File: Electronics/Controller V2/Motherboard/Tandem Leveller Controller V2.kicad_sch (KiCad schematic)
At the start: 6 parts, among them J8 776180-1, J9 776279-1

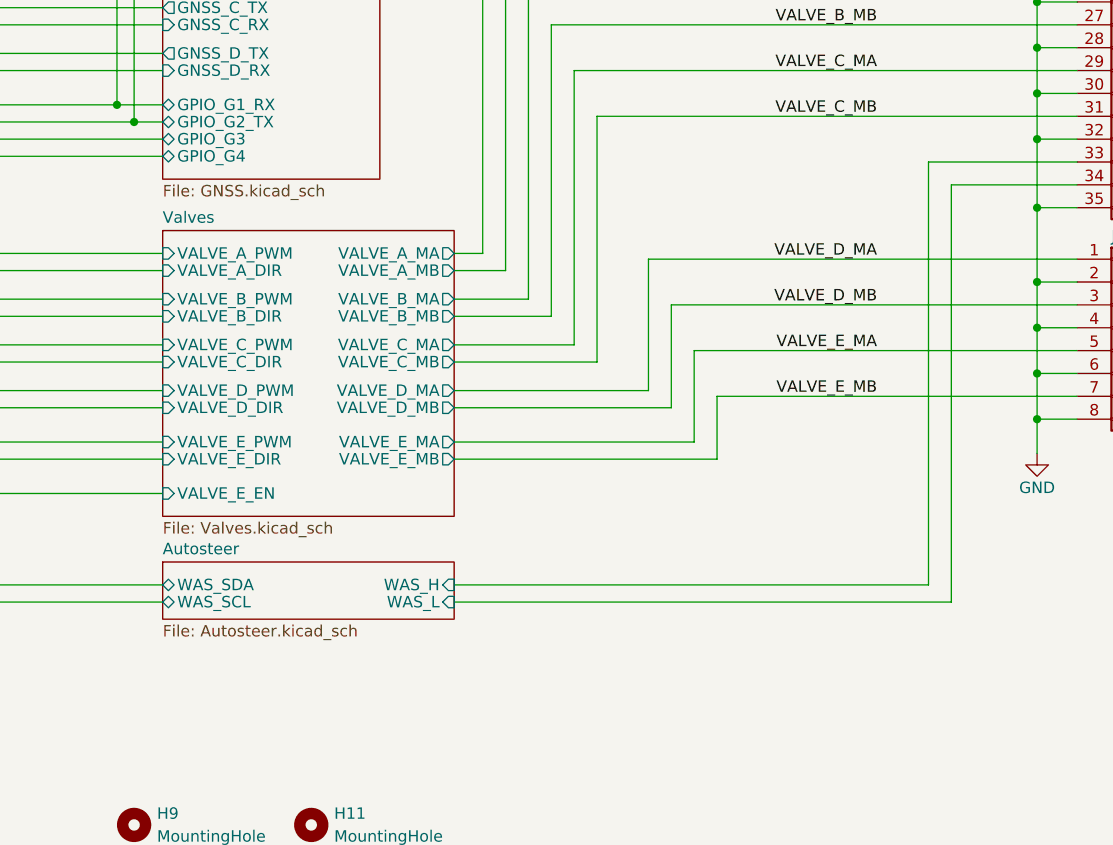
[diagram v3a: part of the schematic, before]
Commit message: Added current sensing for valve E.
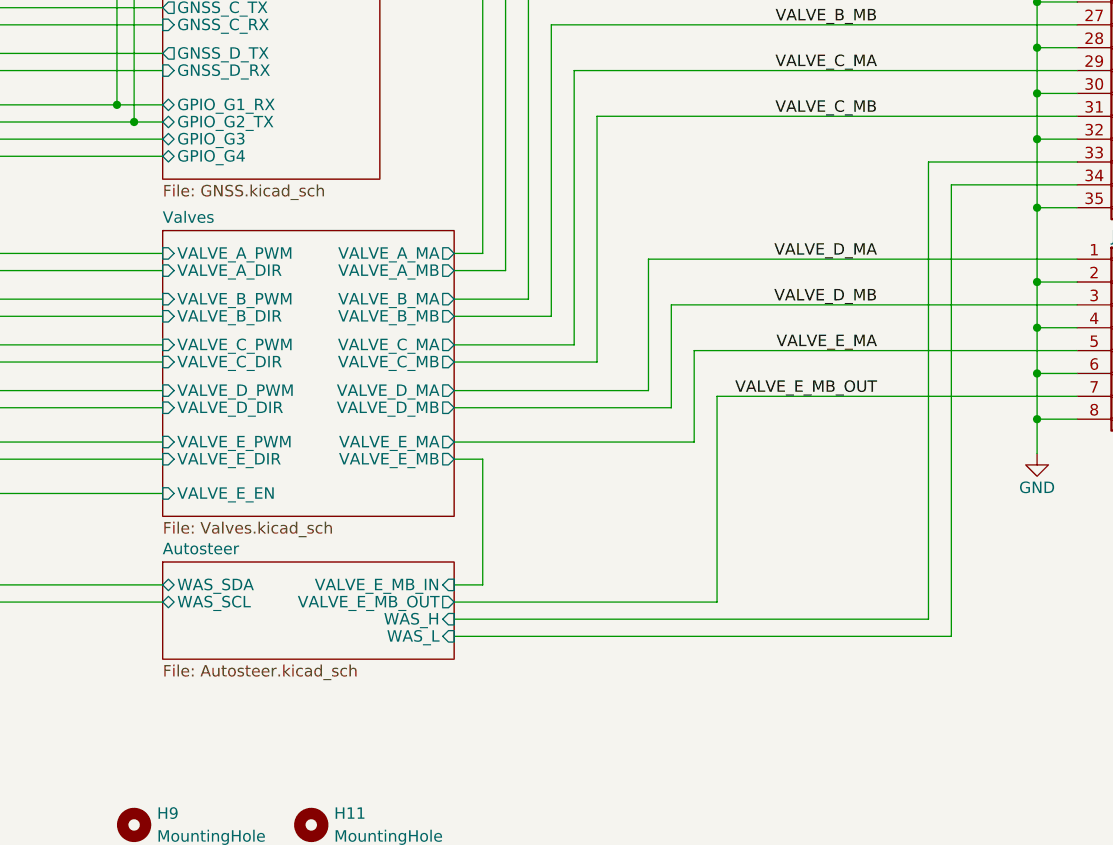
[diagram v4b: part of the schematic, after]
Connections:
- net VALVE_E_MB renamed VALVE_E_MB_OUT
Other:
- sheet Autosteer ports: added VALVE_E_MB_IN, VALVE_E_MB_OUT; removed none
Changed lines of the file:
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@@
     (stroke (width 0) (type default))
   )
-  (wire (pts (xy 222.885 114.3) (xy 222.885 160.655))
+  (wire (pts (xy 222.885 114.3) (xy 222.885 164.465))
     (stroke (width 0) (type default))
   )
@@
     (stroke (width 0) (type default))
   )
+  (wire (pts (xy 167.64 160.655) (xy 196.85 160.655))
+    (stroke (width 0) (type default))
+  )
   (wire (pts (xy 232.41 43.18) (xy 236.855 43.18))
     (stroke (width 0) (type default))
   )
-  (wire (pts (xy 222.885 160.655) (xy 167.64 160.655))
+  (wire (pts (xy 222.885 164.465) (xy 167.64 164.465))
     (stroke (width 0) (type default))
   )
@@
     (stroke (width 0) (type default))
   )
+  (wire (pts (xy 170.815 158.75) (xy 167.64 158.75))
+    (stroke (width 0) (type default))
+  )
   (wire (pts (xy 160.02 38.1) (xy 222.885 38.1))
     (stroke (width 0) (type default))
@@
     (stroke (width 0) (type default))
   )
-  (wire (pts (xy 220.345 111.76) (xy 220.345 158.75))
-    (stroke (width 0) (type default))
-  )
-  (wire (pts (xy 220.345 158.75) (xy 167.64 158.75))
+  (wire (pts (xy 220.345 111.76) (xy 220.345 162.56))
+    (stroke (width 0) (type default))
+  )
+  (wire (pts (xy 220.345 162.56) (xy 167.64 162.56))
     (stroke (width 0) (type default))
   )
@@
     (stroke (width 0) (type default))
   )
+  (wire (pts (xy 170.815 144.78) (xy 170.815 158.75))
+    (stroke (width 0) (type default))
+  )
   (wire (pts (xy 203.835 20.32) (xy 203.835 76.2))
     (stroke (width 0) (type default))
@@
     (stroke (width 0) (type default))
   )
-  (wire (pts (xy 196.85 144.78) (xy 196.85 137.795))
+  (wire (pts (xy 196.85 137.795) (xy 196.85 160.655))
     (stroke (width 0) (type default))
   )
@@
     (stroke (width 0) (type default))
   )
+  (wire (pts (xy 167.64 144.78) (xy 170.815 144.78))
+    (stroke (width 0) (type default))
+  )
   (wire (pts (xy 222.885 58.42) (xy 222.885 48.26))
     (stroke (width 0) (type default))
@@
     (stroke (width 0) (type default))
   )
-  (wire (pts (xy 167.64 144.78) (xy 196.85 144.78))
-    (stroke (width 0) (type default))
-  )
   (wire (pts (xy 173.355 123.825) (xy 173.355 86.36))
     (stroke (width 0) (type default))
@@
     (effects (font (size 1.27 1.27)) (justify right bottom))
   )
-  (label "VALVE_E_MB" (at 214.63 137.795 180) (fields_autoplaced)
+  (label "VALVE_E_MB_OUT" (at 214.63 137.795 180) (fields_autoplaced)
     (effects (font (size 1.27 1.27)) (justify right bottom))
   )
@@
     )
   )
-  (sheet (at 135.255 156.21) (size 32.385 6.35) (fields_autoplaced)
+  (sheet (at 135.255 156.21) (size 32.385 10.795) (fields_autoplaced)
     (stroke (width 0.1524) (type solid))
     (fill (color 0 0 0 0.0000))
@@
       (effects (font (size 1.27 1.27)) (justify left bottom))
     )
-    (property "Sheetfile" "Autosteer.kicad_sch" (at 135.255 163.1446 0)
+    (property "Sheetfile" "Autosteer.kicad_sch" (at 135.255 167.5896 0)
       (effects (font (size 1.27 1.27)) (justify left top))
     )
@@
       (effects (font (size 1.27 1.27)) (justify left))
     )
-    (pin "WAS_H" input (at 167.64 158.75 0)
-      (effects (font (size 1.27 1.27)) (justify right))
-    )
-    (pin "WAS_L" input (at 167.64 160.655 0)
-      (effects (font (size 1.27 1.27)) (justify right))
-    )
+    (pin "WAS_H" input (at 167.64 162.56 0)
+      (effects (font (size 1.27 1.27)) (justify right))
+    )
+    (pin "WAS_L" input (at 167.64 164.465 0)
+      (effects (font (size 1.27 1.27)) (justify right))
+    )
+    (pin "VALVE_E_MB_IN" input (at 167.64 158.75 0)
+      (effects (font (size 1.27 1.27)) (justify right))
+    )
+    (pin "VALVE_E_MB_OUT" output (at 167.64 160.655 0)
+      (effects (font (size 1.27 1.27)) (justify right))
+    )

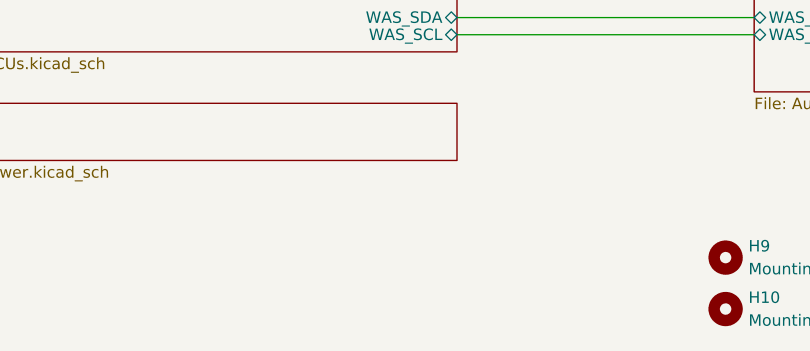
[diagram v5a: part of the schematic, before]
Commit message: Passes rules checks.
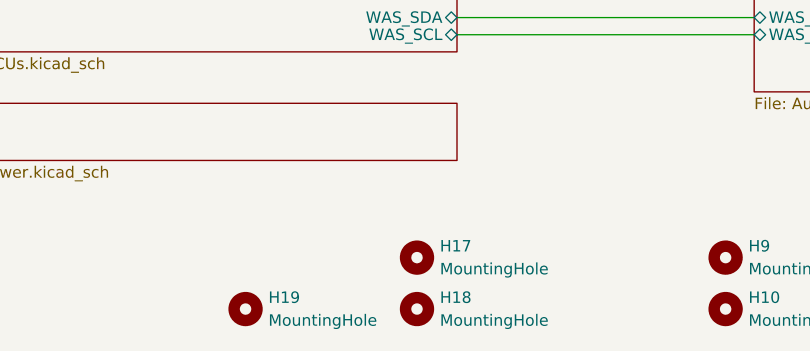
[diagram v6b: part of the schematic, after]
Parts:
- added H17, H18, H19: MountingHole, MountingHole:MountingHole_4mm, symbol Mechanical:MountingHole
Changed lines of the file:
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@@
     (effects (font (size 1.27 1.27)) (justify right bottom))
+  )
+  (symbol (lib_id "Mechanical:MountingHole") (at 97.79 191.135 0) (unit 1)
+    (in_bom yes) (on_board yes) (dnp no) (fields_autoplaced)
+    (property "Reference" "H18" (at 100.33 189.865 0)
+      (effects (font (size 1.27 1.27)) (justify left))
+    )
+    (property "Value" "MountingHole" (at 100.33 192.405 0)
+      (effects (font (size 1.27 1.27)) (justify left))
+    )
+    (property "Footprint" "MountingHole:MountingHole_4mm" (at 97.79 191.135 0)
+      (effects (font (size 1.27 1.27)) hide)
+    )
+    (property "Datasheet" "~" (at 97.79 191.135 0)
+      (effects (font (size 1.27 1.27)) hide)
+    )
+    (instances
+      (project "Tandem Leveller Controller V2"
+        (path "/dceffac9-8f5b-4889-8265-b6c471cb5dde"
+          (reference "H18") (unit 1)
+        )
+      )
+    )
   )
   (symbol (lib_id "Mechanical:MountingHole") (at 132.08 185.42 0) (unit 1)
@@
     )
   )
+  (symbol (lib_id "Mechanical:MountingHole") (at 97.79 185.42 0) (unit 1)
+    (in_bom yes) (on_board yes) (dnp no) (fields_autoplaced)
+    (property "Reference" "H17" (at 100.33 184.15 0)
+      (effects (font (size 1.27 1.27)) (justify left))
+    )
+    (property "Value" "MountingHole" (at 100.33 186.69 0)
+      (effects (font (size 1.27 1.27)) (justify left))
+    )
+    (property "Footprint" "MountingHole:MountingHole_4mm" (at 97.79 185.42 0)
+      (effects (font (size 1.27 1.27)) hide)
+    )
+    (property "Datasheet" "~" (at 97.79 185.42 0)
+      (effects (font (size 1.27 1.27)) hide)
+    )
+    (instances
+      (project "Tandem Leveller Controller V2"
+        (path "/dceffac9-8f5b-4889-8265-b6c471cb5dde"
+          (reference "H17") (unit 1)
+        )
+      )
+    )
+  )
   (symbol (lib_id "power:+5V") (at 229.235 25.4 0) (unit 1)
     (in_bom yes) (on_board yes) (dnp no)
@@
         )
       )
+    )
+  )
+  (symbol (lib_id "Mechanical:MountingHole") (at 78.74 191.135 0) (unit 1)
+    (in_bom yes) (on_board yes) (dnp no) (fields_autoplaced)
+    (property "Reference" "H19" (at 81.28 189.865 0)
+      (effects (font (size 1.27 1.27)) (justify left))
+    )
+    (property "Value" "MountingHole" (at 81.28 192.405 0)
+      (effects (font (size 1.27 1.27)) (justify left))
+    )
+    (property "Footprint" "MountingHole:MountingHole_4mm" (at 78.74 191.135 0)
+      (effects (font (size 1.27 1.27)) hide)
+    )
+    (property "Datasheet" "~" (at 78.74 191.135 0)
+      (effects (font (size 1.27 1.27)) hide)
+    )
+    (instances
+      (project "Tandem Leveller Controller V2"
+        (path "/dceffac9-8f5b-4889-8265-b6c471cb5dde"
+          (reference "H19") (unit 1)
+        )
+      )

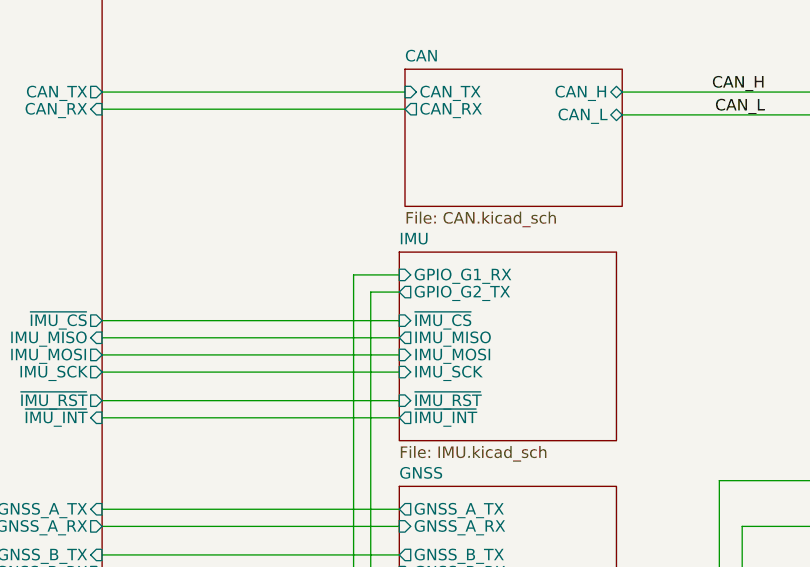
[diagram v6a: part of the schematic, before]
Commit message: Added jumper to bypass current sensing. Minor tweaks. Generated production files.
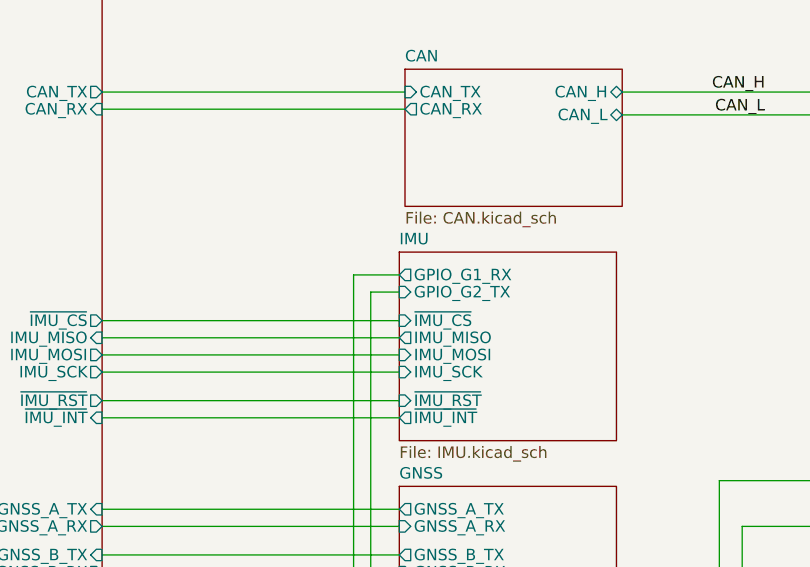
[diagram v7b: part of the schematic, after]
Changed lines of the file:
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@@
       (effects (font (size 1.27 1.27)) (justify left))
     )
-    (pin "GPIO_G2_TX" output (at 135.255 60.325 180)
+    (pin "GPIO_G2_TX" input (at 135.255 60.325 180)
       (effects (font (size 1.27 1.27)) (justify left))
     )
-    (pin "GPIO_G1_RX" input (at 135.255 58.42 180)
+    (pin "GPIO_G1_RX" output (at 135.255 58.42 180)
       (effects (font (size 1.27 1.27)) (justify left))
     )
